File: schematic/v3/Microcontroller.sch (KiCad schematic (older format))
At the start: 29 parts

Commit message: Small cleanup
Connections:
- net labels added: CHARGE_STATUS
- net labels removed: charge_status
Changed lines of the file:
@@
 	6800 4650 6650 4650
 Text HLabel 6800 4650 2    50   Input ~ 0
-charge_status
+CHARGE_STATUS
 Text HLabel 7600 3550 2    50   Input ~ 0
 UART_RN_OUT

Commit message: Started PCB layout
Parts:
- added C11: 100nF, Capacitors_SMD:C_0805, symbol Device:C
- C10, C14, C15, C16, C17, C20, C6, C7, C8, C9: renamed from C?; footprint (none) -> Capacitors_SMD:C_0805
- D3, D4: renamed from D?; footprint (none) -> LEDs:LED_0805_HandSoldering
- R11, R15, R16, R4, R5, R6: renamed from R?; footprint (none) -> Resistors_SMD:R_0805
- R12, R13: renamed from R?; value R -> 1k; footprint (none) -> Resistors_SMD:R_0805
- gave numbers to parts that had none: 9
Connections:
- net labels removed: V_bak
- wire segments 142 -> 146
- no-connect marks 13 -> 14

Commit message: Started layout work
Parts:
- C10, C11, C14, C15, C16, C17, C20, C6, C7, C8, C9: symbol Device:C -> gps_node-rescue:C-Device
- D3, D4: symbol Device:LED -> gps_node-rescue:LED-Device
- R11, R12, R13, R15, R16, R4, R5, R6: symbol Device:R -> gps_node-rescue:R-Device
- SW2, SW3: footprint (none) -> Buttons_Switches_SMD:SW_SPST_PTS645; symbol Switch:SW_Push -> gps_node-rescue:SW_Push-Switch
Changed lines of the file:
@@
 $EndComp
 $Comp
-L power:VBUS #PWR?
+L gps_node-rescue:VBUS-power #PWR?
 U 1 1 5C0B22C9
 P 1950 1200
@@
 $EndComp
 $Comp
-L power:GND #PWR?
+L gps_node-rescue:GND-power #PWR?
 U 1 1 5C0B22DD
 P 1100 1950
@@
 $EndComp
 $Comp
-L power:GND #PWR?
+L gps_node-rescue:GND-power #PWR?
 U 1 1 5C0B2301
 P 1500 3850
@@
 $EndComp
 $Comp
-L power:GND #PWR?
+L gps_node-rescue:GND-power #PWR?
 U 1 1 5C0B231D
 P 3500 2850
@@
 $EndComp
 $Comp
-L power:VBUS #PWR?
+L gps_node-rescue:VBUS-power #PWR?
 U 1 1 5C0B2323
 P 4300 3300
@@
 USBD-
 $Comp
-L power:+3V3 #PWR?
+L gps_node-rescue:+3V3-power #PWR?
 U 1 1 5C0B233F
 P 10250 1300
@@
 $EndComp
 $Comp
-L power:VBUS #PWR?
+L gps_node-rescue:VBUS-power #PWR?
 U 1 1 5C0B2345
 P 5100 1850
@@
 $EndComp
 $Comp
-L power:GND #PWR?
+L gps_node-rescue:GND-power #PWR?
 U 1 1 5C0B2352
 P 4200 4900
@@
 $EndComp
 $Comp
-L power:GND #PWR?
+L gps_node-rescue:GND-power #PWR?
 U 1 1 5C0B2358
 P 5200 5400
@@
 $EndComp
 $Comp
-L power:+3V3 #PWR?
+L gps_node-rescue:+3V3-power #PWR?
 U 1 1 5C0B235E
 P 5550 1800
@@
 $EndComp
 $Comp
-L power:GND #PWR?
+L gps_node-rescue:GND-power #PWR?
 U 1 1 5C0B2379
 P 10250 2250
@@
 MISO
 $Comp
-L power:+3V3 #PWR?
+L gps_node-rescue:+3V3-power #PWR?
 U 1 1 5C0B2385
 P 9250 1550
@@
 RESET
 $Comp
-L power:GND #PWR?
+L gps_node-rescue:GND-power #PWR?
 U 1 1 5C0B238E
 P 9250 1850
@@
 $EndComp
 $Comp
-L power:GND #PWR?
+L gps_node-rescue:GND-power #PWR?
 U 1 1 5C0B23AE
 P 1600 7050
@@
 $EndComp
 $Comp
-L power:GND #PWR?
+L gps_node-rescue:GND-power #PWR?
 U 1 1 5C0B23BF
 P 2900 7050
@@
 	2900 7000 3000 7000
 $Comp
-L power:GND #PWR?
+L gps_node-rescue:GND-power #PWR?
 U 1 1 5C0B2437
 P 9100 4450
@@
 $EndComp
 $Comp
-L power:+3V3 #PWR?
+L gps_node-rescue:+3V3-power #PWR?
 U 1 1 5C0B243D
 P 9100 3500
@@
 LED0
 $Comp
-L power:GND #PWR?
+L gps_node-rescue:GND-power #PWR?
 U 1 1 5C0B245D
 P 1850 5700
@@
 $EndComp
 $Comp
-L power:GND #PWR?
+L gps_node-rescue:GND-power #PWR?
 U 1 1 5C0B2463
 P 1500 5700
@@
 	2600 1400 2350 1400
 $Comp
-L power:+3V3 #PWR?
+L gps_node-rescue:+3V3-power #PWR?
 U 1 1 5C0D179B
 P 9250 5700
@@
 GND
 $Comp
-L power:GND #PWR?
+L gps_node-rescue:GND-power #PWR?
 U 1 1 5C0D17A6
 P 8950 6200
@@
 V_BAK
 $Comp
-L power:VBUS #PWR?
+L gps_node-rescue:VBUS-power #PWR?
 U 1 1 5C0D17AF
 P 9100 5550
@@
 $EndComp
 $Comp
-L power:+BATT #PWR?
+L gps_node-rescue:+BATT-power #PWR?
 U 1 1 5C0D17B5
 P 8950 5400
@@
 	1500 4950 1500 5000
 $Comp
-L Device:LED D4
+L gps_node-rescue:LED-Device D4
 U 1 1 5C0EB197
 P 1500 5500
@@
 $EndComp
 $Comp
-L Device:LED D3
+L gps_node-rescue:LED-Device D3
 U 1 1 5C0F02A8
 P 1850 5500
@@
 $EndComp
 $Comp
-L Device:R R13
+L gps_node-rescue:R-Device R13
 U 1 1 5C0F2C2B
 P 1500 5150
@@
 $EndComp
 $Comp
-L Device:R R12
+L gps_node-rescue:R-Device R12
 U 1 1 5C0F2C85
 P 1850 5150
@@
 LED0 : GPS Lock\nLED1: Transmitting
 $Comp
-L Device:R R16
+L gps_node-rescue:R-Device R16
 U 1 1 5C10FDBE
 P 1500 3600
@@
 $EndComp
 $Comp
-L Device:C C20
+L gps_node-rescue:C-Device C20
 U 1 1 5C112AF4
 P 1300 3600
@@
 	1300 3450 1300 3300
 $Comp
-L Device:R R15
+L gps_node-rescue:R-Device R15
 U 1 1 5C1186D1
 P 1500 3050
@@
 Connection ~ 1500 3850
 $Comp
-L power:+BATT #PWR?
+L gps_node-rescue:+BATT-power #PWR?
 U 1 1 5C0B23CD
 P 1500 2800
@@
 	1500 3300 1500 3200
 $Comp
-L Device:R R4
+L gps_node-rescue:R-Device R4
 U 1 1 5C13754C
 P 2200 1400
@@
 $EndComp
 $Comp
-L Device:R R5
+L gps_node-rescue:R-Device R5
 U 1 1 5C137961
 P 2200 1600
@@
 	7250 5050 6650 5050
 $Comp
-L Device:C C17
+L gps_node-rescue:C-Device C17
 U 1 1 5C1D04D9
 P 4200 4700
@@
 	4200 4900 4200 4850
 $Comp
-L Device:C C16
+L gps_node-rescue:C-Device C16
 U 1 1 5C1D900B
 P 4200 3900
@@
 $EndComp
 $Comp
-L power:GND #PWR?
+L gps_node-rescue:GND-power #PWR?
 U 1 1 5C1D952D
 P 4200 4100
@@
 	3500 2500 3500 2800
 $Comp
-L Device:C C15
+L gps_node-rescue:C-Device C15
 U 1 1 5C1F431D
 P 3800 2800
@@
 $EndComp
 $Comp
-L Device:C C14
+L gps_node-rescue:C-Device C14
 U 1 1 5C1F470E
 P 3800 2500
@@
 	3950 2500 4200 2500
 $Comp
-L Device:R R6
+L gps_node-rescue:R-Device R6
 U 1 1 5C208D59
 P 10250 1550
@@
 	3950 2150 4400 2150
 $Comp
-L Device:R R11
+L gps_node-rescue:R-Device R11
 U 1 1 5C22B52E
 P 9100 3700
@@
 	8550 3900 9100 3900
 $Comp
-L Switch:SW_Push SW3
+L gps_node-rescue:SW_Push-Switch SW3
 U 1 1 5C2372FF
 P 9100 4150
 F 0 "SW3" V 9054 4298 50  0000 L CNN
 F 1 "SW_Push" V 9145 4298 50  0000 L CNN
-F 2 "" H 9100 4350 50  0001 C CNN
+F 2 "Buttons_Switches_SMD:SW_SPST_PTS645" H 9100 4350 50  0001 C CNN
 F 3 "" H 9100 4350 50  0001 C CNN
 	1    9100 4150
@@
 Connection ~ 9100 3900
 $Comp
-L Switch:SW_Push SW2
+L gps_node-rescue:SW_Push-Switch SW2
 U 1 1 5C242BA0
 P 10250 2000
 F 0 "SW2" V 10204 2148 50  0000 L CNN
 F 1 "SW_Push" V 10295 2148 50  0000 L CNN
-F 2 "" H 10250 2200 50  0001 C CNN
+F 2 "Buttons_Switches_SMD:SW_SPST_PTS645" H 10250 2200 50  0001 C CNN
 F 3 "" H 10250 2200 50  0001 C CNN
 	1    10250 2000
@@
 	1300 6900 1700 6900
 $Comp
-L power:+3V3 #PWR?
+L gps_node-rescue:+3V3-power #PWR?
 U 1 1 5C2C185A
 P 4600 6600
@@
 $EndComp
 $Comp
-L power:GND #PWR?
+L gps_node-rescue:GND-power #PWR?
 U 1 1 5C2C1B7D
 P 4600 7100
@@
 $EndComp
 $Comp
-L Device:C C6
+L gps_node-rescue:C-Device C6
 U 1 1 5C2C276B
 P 4600 6850
@@
 $EndComp
 $Comp
-L Device:C C7
+L gps_node-rescue:C-Device C7
 U 1 1 5C2FC909
 P 5100 6850
@@
 $EndComp
 $Comp
-L Device:C C8
+L gps_node-rescue:C-Device C8
 U 1 1 5C2FC969
 P 5400 6850
@@
 $EndComp
 $Comp
-L Device:C C9
+L gps_node-rescue:C-Device C9
 U 1 1 5C2FC9B7
 P 5700 6850
@@
 $EndComp
 $Comp
-L Device:C C10
+L gps_node-rescue:C-Device C10
 U 1 1 5C2FCA64
 P 6000 6850
@@
 NoConn ~ 6650 2550
 $Comp
-L Device:C C11
+L gps_node-rescue:C-Device C11
 U 1 1 5BE580E5
 P 6300 6850

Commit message: Adds Accelerometer, layout almost done
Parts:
- added TP1, TP2, TP3, TP4, TP5, TP6, TP7, TP8: TestPoint, test_pad:test_pad, symbol Connector:TestPoint
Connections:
- net labels added: ACCEL_CS, ACCEL_INT, SPI_CLK, SPI_MISO, SPI_MOSI
- wire segments 146 -> 156
- no-connect marks 14 -> 4
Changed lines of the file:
@@
 $Descr A4 11693 8268
 encoding utf-8
-Sheet 3 4
+Sheet 3 5
 Title ""
 Date ""
@@
 Text Label 6800 5050 0    60   ~ 0
 LED1
-NoConn ~ 6650 4850
 NoConn ~ 6650 4250
-NoConn ~ 6650 3150
 NoConn ~ 6650 2150
 $Comp
@@
 Text HLabel 7600 3650 2    50   Output ~ 0
 UART_RN_IN
-Text HLabel 6800 3050 2    50   Output ~ 0
+Text HLabel 7600 3050 2    50   Output ~ 0
 RN_RESET
 Wire Wire Line
-	6800 3050 6650 3050
+	7600 3050 6650 3050
 Wire Wire Line
 	7600 3550 6650 3550
@@
 SCK
 Wire Wire Line
-	6650 2250 7250 2250
-Wire Wire Line
-	6650 2350 7250 2350
-Wire Wire Line
-	6650 2450 7250 2450
+	6650 2250 7600 2250
+Wire Wire Line
+	6650 2350 7600 2350
+Wire Wire Line
+	6650 2450 7600 2450
 Text Label 6800 2350 0    60   ~ 0
 MOSI
@@
 Text Notes 4350 6300 0    101  ~ 0
 Decoupling Capacitors
-NoConn ~ 6650 2850
-NoConn ~ 6650 3450
-NoConn ~ 6650 3750
-NoConn ~ 6650 3850
-NoConn ~ 6650 3950
-NoConn ~ 6650 4050
 NoConn ~ 6650 4350
-NoConn ~ 6650 4750
-NoConn ~ 6650 2550
 $Comp
 L gps_node-rescue:C-Device C11
@@
 	6300 7050 6300 7000
 Connection ~ 6000 7050
+Wire Wire Line
+	6750 3750 6650 3750
+Wire Wire Line
+	6650 3850 6750 3850
+Wire Wire Line
+	6750 3950 6650 3950
+Wire Wire Line
+	6650 4050 6750 4050
+$Comp
+L Connector:TestPoint TP3
+U 1 1 5BE8DCB2
+P 6750 3750
+F 0 "TP3" V 6750 3950 50  0000 L CNN
+F 1 "TestPoint" V 6750 4150 50  0000 L CNN
+F 2 "test_pad:test_pad" H 6950 3750 50  0001 C CNN
+F 3 "~" H 6950 3750 50  0001 C CNN
+	1    6750 3750
+	0    1    1    0
+$EndComp
+$Comp
+L Connector:TestPoint TP4
+U 1 1 5BE8DF17
+P 6750 3850
+F 0 "TP4" V 6750 4050 50  0000 L CNN
+F 1 "TestPoint" V 6750 4250 50  0000 L CNN
+F 2 "test_pad:test_pad" H 6950 3850 50  0001 C CNN
+F 3 "~" H 6950 3850 50  0001 C CNN
+	1    6750 3850
+	0    1    1    0
+$EndComp
+$Comp
+L Connector:TestPoint TP7
+U 1 1 5BE8DF67
+P 6750 4750
+F 0 "TP7" V 6750 4950 50  0000 L CNN
+F 1 "TestPoint" V 6750 5150 50  0000 L CNN
+F 2 "test_pad:test_pad" H 6950 4750 50  0001 C CNN
+F 3 "~" H 6950 4750 50  0001 C CNN
+	1    6750 4750
+	0    1    1    0
+$EndComp
+$Comp
+L Connector:TestPoint TP5
+U 1 1 5BE8DFBF
+P 6750 3950
+F 0 "TP5" V 6750 4150 50  0000 L CNN
+F 1 "TestPoint" V 6750 4350 50  0000 L CNN
+F 2 "test_pad:test_pad" H 6950 3950 50  0001 C CNN
+F 3 "~" H 6950 3950 50  0001 C CNN
+	1    6750 3950
+	0    1    1    0
+$EndComp
+$Comp
+L Connector:TestPoint TP6
+U 1 1 5BE8E00F
+P 6750 4050
+F 0 "TP6" V 6750 4250 50  0000 L CNN
+F 1 "TestPoint" V 6750 4450 50  0000 L CNN
+F 2 "test_pad:test_pad" H 6950 4050 50  0001 C CNN
+F 3 "~" H 6950 4050 50  0001 C CNN
+	1    6750 4050
+	0    1    1    0
+$EndComp
+$Comp
+L Connector:TestPoint TP8
+U 1 1 5BE8E138
+P 6750 4850
+F 0 "TP8" V 6750 5050 50  0000 L CNN
+F 1 "TestPoint" V 6750 5250 50  0000 L CNN
+F 2 "test_pad:test_pad" H 6950 4850 50  0001 C CNN
+F 3 "~" H 6950 4850 50  0001 C CNN
+	1    6750 4850
+	0    1    1    0
+$EndComp
+Wire Wire Line
+	6750 4750 6650 4750
+Wire Wire Line
+	6650 4850 6750 4850
+Wire Wire Line
+	6650 3450 7600 3450
+Text HLabel 7600 3450 2    50   Input ~ 0
+ACCEL_INT
+Text HLabel 7600 2250 2    50   Output ~ 0
+SPI_CLK
+Text HLabel 7600 2350 2    50   Output ~ 0
+SPI_MOSI
+Text HLabel 7600 2450 2    50   Input ~ 0
+SPI_MISO
+Text HLabel 7600 3150 2    50   Output ~ 0
+ACCEL_CS
+Wire Wire Line
+	7600 3150 6650 3150
+$Comp
+L Connector:TestPoint TP2
+U 1 1 5BECA5FF
+P 6750 2850
+F 0 "TP2" V 6750 3050 50  0000 L CNN
+F 1 "TestPoint" V 6750 3250 50  0000 L CNN
+F 2 "test_pad:test_pad" H 6950 2850 50  0001 C CNN
+F 3 "~" H 6950 2850 50  0001 C CNN
+	1    6750 2850
+	0    1    1    0
+$EndComp
+$Comp
+L Connector:TestPoint TP1
+U 1 1 5BECA6BD
+P 6750 2550
+F 0 "TP1" V 6750 2750 50  0000 L CNN
+F 1 "TestPoint" V 6750 2950 50  0000 L CNN
+F 2 "test_pad:test_pad" H 6950 2550 50  0001 C CNN
+F 3 "~" H 6950 2550 50  0001 C CNN
+	1    6750 2550
+	0    1    1    0
+$EndComp
+Wire Wire Line
+	6750 2550 6650 2550
+Wire Wire Line
+	6650 2850 6750 2850
 $EndSCHEMATC

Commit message: Fixed battery connector, started bom
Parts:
- TP1, TP2, TP3, TP4, TP5, TP6, TP7, TP8: symbol Connector:TestPoint -> gps_node-rescue:TestPoint-Connector
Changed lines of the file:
@@
 	6650 4050 6750 4050
 $Comp
-L Connector:TestPoint TP3
+L gps_node-rescue:TestPoint-Connector TP3
 U 1 1 5BE8DCB2
 P 6750 3750
@@
 $EndComp
 $Comp
-L Connector:TestPoint TP4
+L gps_node-rescue:TestPoint-Connector TP4
 U 1 1 5BE8DF17
 P 6750 3850
@@
 $EndComp
 $Comp
-L Connector:TestPoint TP7
+L gps_node-rescue:TestPoint-Connector TP7
 U 1 1 5BE8DF67
 P 6750 4750
@@
 $EndComp
 $Comp
-L Connector:TestPoint TP5
+L gps_node-rescue:TestPoint-Connector TP5
 U 1 1 5BE8DFBF
 P 6750 3950
@@
 $EndComp
 $Comp
-L Connector:TestPoint TP6
+L gps_node-rescue:TestPoint-Connector TP6
 U 1 1 5BE8E00F
 P 6750 4050
@@
 $EndComp
 $Comp
-L Connector:TestPoint TP8
+L gps_node-rescue:TestPoint-Connector TP8
 U 1 1 5BE8E138
 P 6750 4850
@@
 	7600 3150 6650 3150
 $Comp
-L Connector:TestPoint TP2
+L gps_node-rescue:TestPoint-Connector TP2
 U 1 1 5BECA5FF
 P 6750 2850
@@
 $EndComp
 $Comp
-L Connector:TestPoint TP1
+L gps_node-rescue:TestPoint-Connector TP1
 U 1 1 5BECA6BD
 P 6750 2550

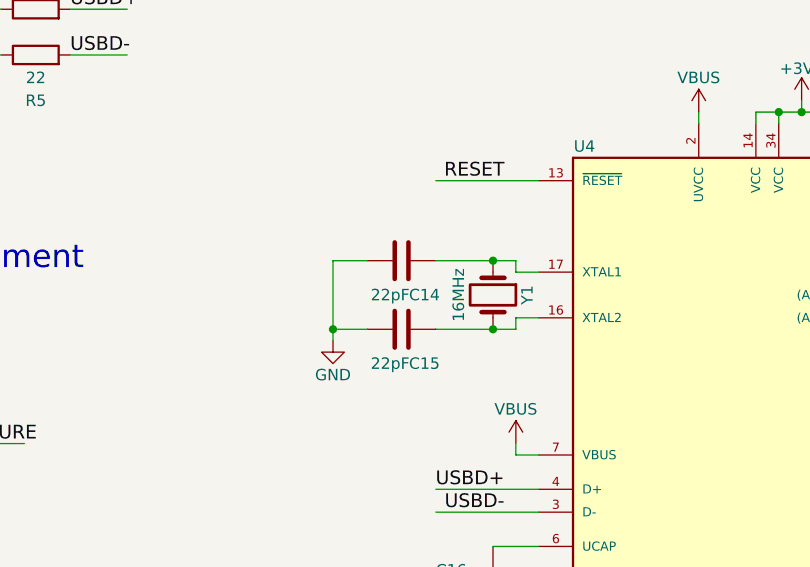
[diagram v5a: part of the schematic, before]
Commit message: Update BOM, so old components
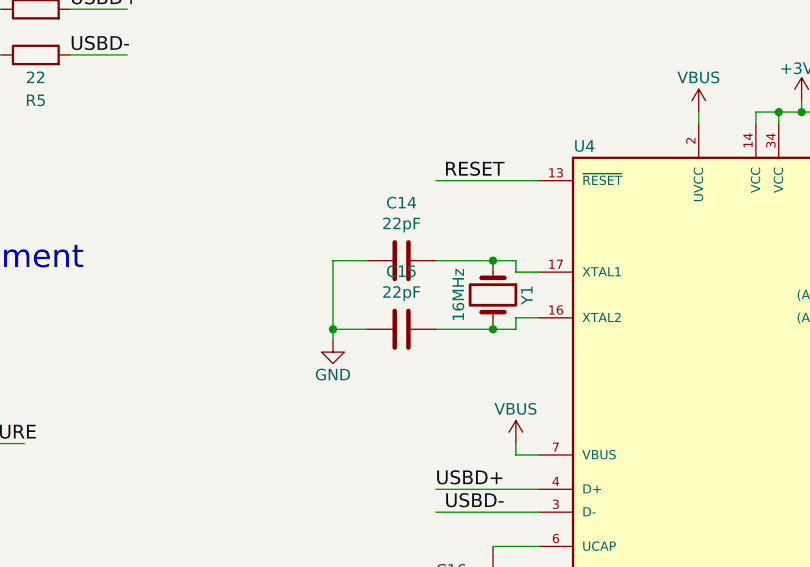
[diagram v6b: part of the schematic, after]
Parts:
- removed C14, C15: 22pF, Capacitors_SMD:C_0805, symbol gps_node-rescue:C-Device
- added C14, C15: 22pF, symbol Device:C
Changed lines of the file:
@@
 Wire Wire Line
 	3500 2500 3500 2800
-$Comp
-L gps_node-rescue:C-Device C15
-U 1 1 5C1F431D
-P 3800 2800
-F 0 "C15" V 3950 2700 50  0000 C CNN
-F 1 "22pF" V 3950 2850 50  0000 C CNN
-F 2 "Capacitors_SMD:C_0805" H 3838 2650 50  0001 C CNN
-F 3 "~" H 3800 2800 50  0001 C CNN
-	1    3800 2800
-	0    -1   1    0
-$EndComp
-$Comp
-L gps_node-rescue:C-Device C14
-U 1 1 5C1F470E
-P 3800 2500
-F 0 "C14" V 3950 2400 50  0000 C CNN
-F 1 "22pF" V 3950 2550 50  0000 C CNN
-F 2 "Capacitors_SMD:C_0805" H 3838 2350 50  0001 C CNN
-F 3 "~" H 3800 2500 50  0001 C CNN
-	1    3800 2500
-	0    -1   1    0
-$EndComp
 Wire Wire Line
 	3650 2500 3500 2500
@@
 Wire Wire Line
 	6650 2850 6750 2850
+$Comp
+L Device:C C14
+U 1 1 5BE93B6E
+P 3800 2500
+F 0 "C14" V 3548 2500 50  0000 C CNN
+F 1 "22pF" V 3639 2500 50  0000 C CNN
+F 2 "" H 3838 2350 50  0001 C CNN
+F 3 "~" H 3800 2500 50  0001 C CNN
+	1    3800 2500
+	0    1    1    0
+$EndComp
+$Comp
+L Device:C C15
+U 1 1 5BE93C1E
+P 3800 2800
+F 0 "C15" V 3548 2800 50  0000 C CNN
+F 1 "22pF" V 3639 2800 50  0000 C CNN
+F 2 "" H 3838 2650 50  0001 C CNN
+F 3 "~" H 3800 2800 50  0001 C CNN
+	1    3800 2800
+	0    1    1    0
+$EndComp
 $EndSCHEMATC

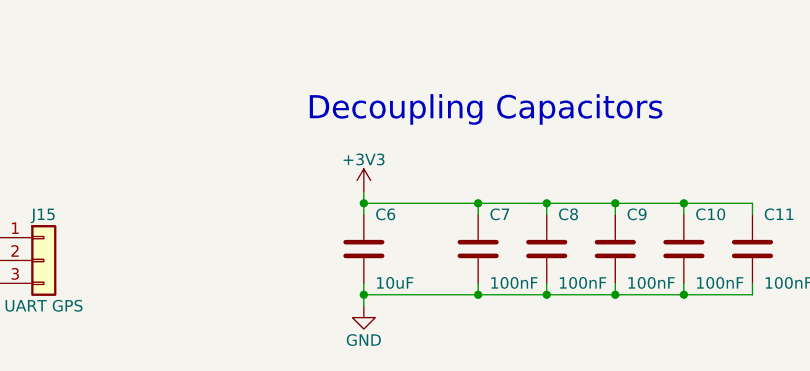
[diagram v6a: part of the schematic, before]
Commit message: Replace 10uF by 4.7uF and clean up power circuit
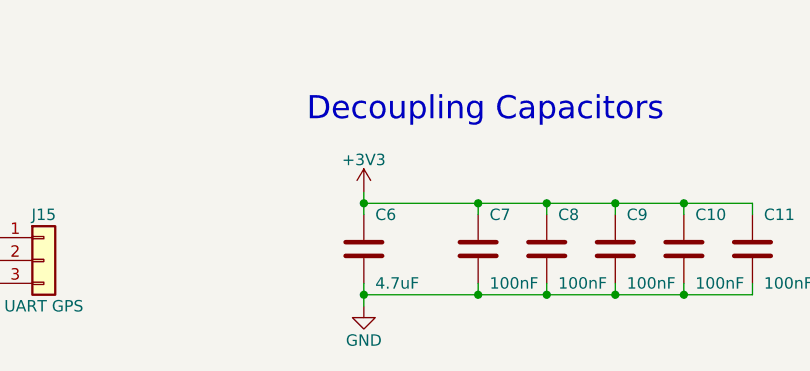
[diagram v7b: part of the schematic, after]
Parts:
- C6: value 10uF -> 4.7uF
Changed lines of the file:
@@
 P 4600 6850
 F 0 "C6" H 4650 7000 50  0000 L CNN
-F 1 "10uF" H 4650 6700 50  0000 L CNN
+F 1 "4.7uF" H 4650 6700 50  0000 L CNN
 F 2 "Capacitors_SMD:C_0805" H 4638 6700 50  0001 C CNN
 F 3 "~" H 4600 6850 50  0001 C CNN
